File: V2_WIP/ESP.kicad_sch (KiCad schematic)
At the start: 41 parts, among them J202 USB4145-03-0230-C, J3 BATT, Q1 IRLML5203, Q2 S8050, Q3 S8050, SW3 FSM14JLH, SW4 FSM14JLH, U1 ESP32-WROOM-32E, U13 TP4057, U14 CH340K, U201 RT9080

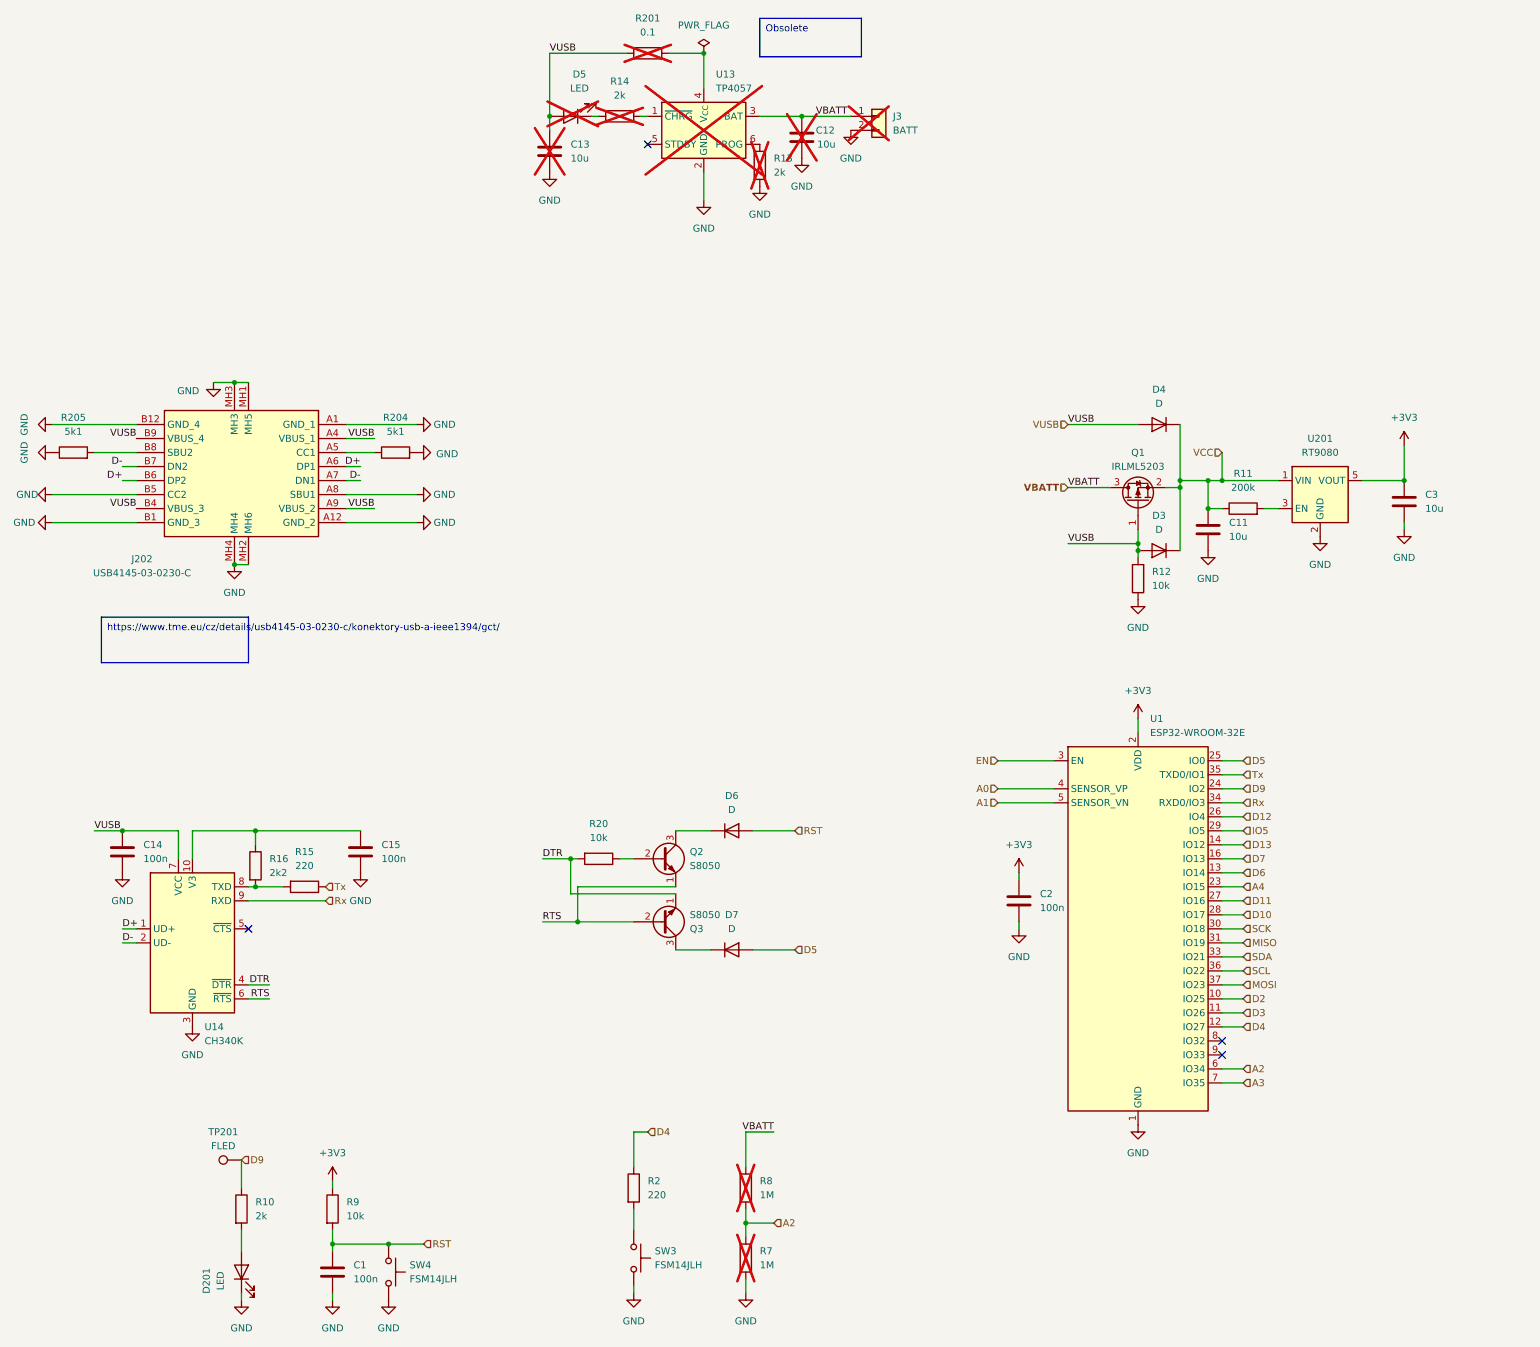
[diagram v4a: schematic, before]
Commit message: Removed EEPROM, Adjusted Flash connection, renamed ESP pins and several other signals
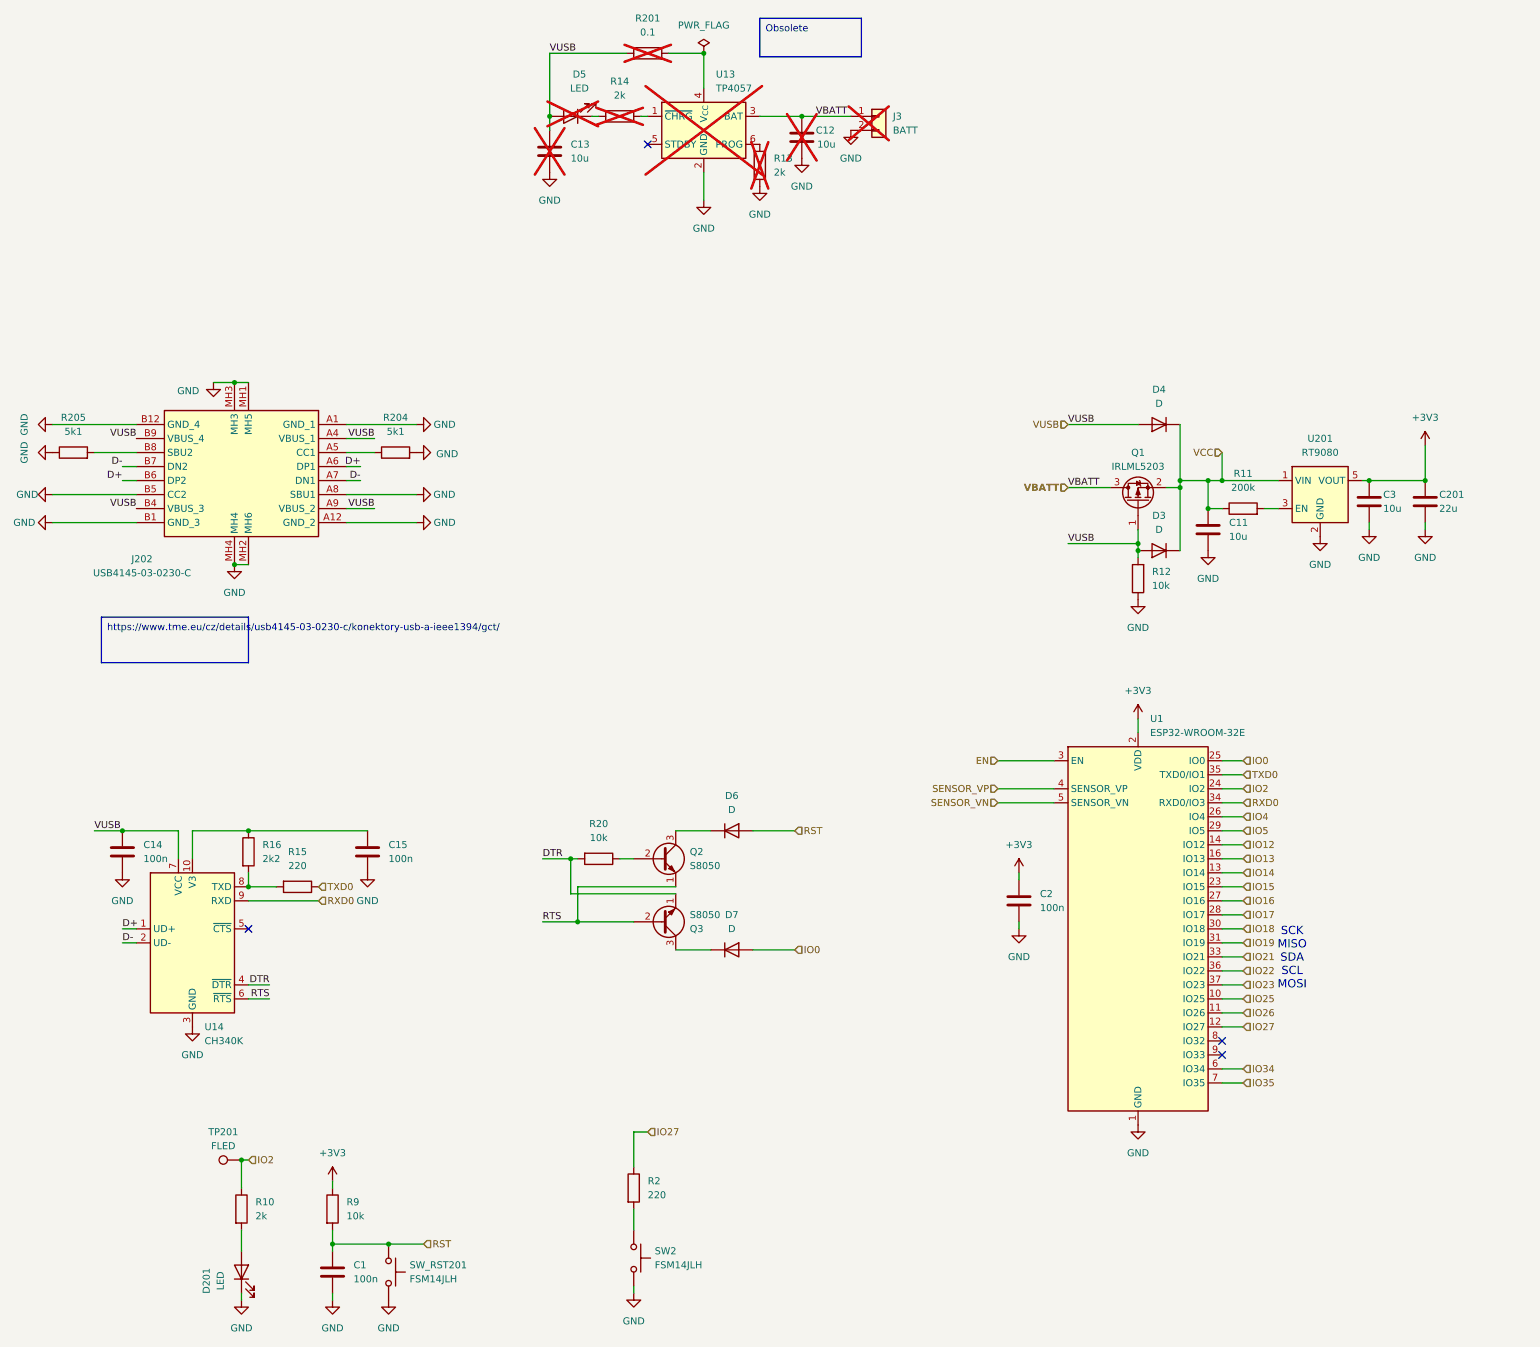
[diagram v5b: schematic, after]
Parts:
- removed R7, R8: 1M, Resistor_SMD:R_0603_1608Metric_Pad0.98x0.95mm_HandSolder, symbol Device:R
- added C201: 22u, Capacitor_SMD:C_0603_1608Metric_Pad1.08x0.95mm_HandSolder, symbol Device:C
- renumbered SW3 to SW2, SW4 to SW_RST201
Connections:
- net +3V3: now also C201.1
- net GND: now also C201.2
- net A0 renamed SENSOR_VP
- net A1 renamed SENSOR_VN
- net A2 renamed IO34
- net A3 renamed IO35
- net A4 renamed IO15
- net D10 renamed IO17
- net D11 renamed IO16
- net D12 renamed IO4
- net D13 renamed IO12
- net D2 renamed IO25
- net D3 renamed IO26
- net D4 renamed IO27
- net D5 renamed IO0
- net D6 renamed IO14
- net D7 renamed IO13
- net D9 renamed IO2
- net MISO renamed IO19
- net MOSI renamed IO23
- net Rx renamed RXD0
- net SCK renamed IO18
- net SCL renamed IO22
- net SDA renamed IO21
- net Tx renamed TXD0
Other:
- note added: "SCK MISO SDA SCL MOSI"
- moved on the sheet: C15, C3, R15, R16

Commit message: minor changes
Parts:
- removed SW_RST201: FSM14JLH, Button_Switch_THT:SW_PUSH_6mm, symbol Switch:SW_Push
- added R202: Manual rst, Resistor_SMD:R_0603_1608Metric_Pad0.98x0.95mm_HandSolder, symbol Device:R
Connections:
- net GND: now also R202.2
- net RST: now also R202.1
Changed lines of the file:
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@@
 	(wire
 		(pts
-			(xy 90.17 173.99) (xy 83.82 173.99)
-		)
-		(stroke
-			(width 0)
-			(type default)
-		)
-	)
-	(wire
-		(pts
 			(xy 234.95 129.54) (xy 238.76 129.54)
 		)
@@
 	(wire
 		(pts
+			(xy 83.82 175.26) (xy 83.82 173.99)
+		)
+		(stroke
+			(width 0)
+			(type default)
+		)
+	)
+	(wire
+		(pts
 			(xy 234.95 104.14) (xy 238.76 104.14)
 		)
@@
 	(wire
 		(pts
+			(xy 83.82 182.88) (xy 83.82 184.15)
+		)
+		(stroke
+			(width 0)
+			(type default)
+		)
+	)
+	(wire
+		(pts
 			(xy 45.72 99.06) (xy 45.72 104.14)
 		)
@@
 	(wire
 		(pts
+			(xy 83.82 173.99) (xy 90.17 173.99)
+		)
+		(stroke
+			(width 0)
+			(type default)
+		)
+	)
+	(wire
+		(pts
 			(xy 234.95 96.52) (xy 238.76 96.52)
 		)
@@
 		(exclude_from_sim no)
 		(at 31.75 60.325 0)
-		(size 26.67 8.255)
+		(size 89.154 8.255)
+		(stroke
+			(width 0)
+			(type default)
+		)
+		(fill
+			(type none)
+		)
+		(effects
+			(font
+				(size 1.27 1.27)
+			)
+			(justify left top)
+		)
+	)
+	(text_box "Manual rst possible by shorting R202"
+		(exclude_from_sim no)
+		(at 79.756 162.306 0)
+		(size 17.78 9.398)
 		(stroke
 			(width 0)
@@
 	)
 	(symbol
-		(lib_id "power:GND")
-		(at 151.13 -17.78 0)
+		(lib_id "Device:R")
+		(at 83.82 179.07 0)
 		(unit 1)
 		(exclude_from_sim no)
 		(in_bom yes)
 		(on_board yes)
-		(dnp no)
+		(dnp yes)
 		(fields_autoplaced yes)
-		(property "Reference" "#PWR0108"
-			(at 151.13 -11.43 0)
+		(property "Reference" "R202"
+			(at 86.36 177.7999 0)
 			(effects
 				(font
 					(size 1.27 1.27)
 				)
-				(hide yes)
+				(justify left)
 			)
 		)
-		(property "Value" "GND"
-			(at 151.13 -12.7 0)
+		(property "Value" "Manual rst"
+			(at 86.36 180.3399 0)
 			(effects
 				(font
 					(size 1.27 1.27)
 				)
+				(justify left)
 			)
 		)
-		(property "Footprint" ""
-			(at 151.13 -17.78 0)
+		(property "Footprint" "Resistor_SMD:R_0603_1608Metric_Pad0.98x0.95mm_HandSolder"
+			(at 82.042 179.07 90)
 			(effects
 				(font
@@
 			)
 		)
-		(property "Datasheet" ""
-			(at 151.13 -17.78 0)
+		(property "Datasheet" "~"
+			(at 83.82 179.07 0)
 			(effects
 				(font
@@
 			)
 		)
-		(property "Description" "Power symbol creates a global label with name \"GND\" , ground"
-			(at 151.13 -17.78 0)
+		(property "Description" "Resistor"
+			(at 83.82 179.07 0)
 			(effects
 				(font
@@
 		(pin "1"
 		)
+		(pin "2"
+		)
 		(instances
 			(project "gps"
 				(path "/00526ddc-5304-4072-af1e-192a9e7e83da/9ca8f2f0-17b3-4db3-a6cc-93c49e56ea8b"
-					(reference "#PWR0108")
+					(reference "R202")
 					(unit 1)
 				)
@@
 	(symbol
 		(lib_id "power:GND")
-		(at 232.41 48.26 0)
+		(at 151.13 -17.78 0)
 		(unit 1)
 		(exclude_from_sim no)
@@
 		(dnp no)
 		(fields_autoplaced yes)
-		(property "Reference" "#PWR0103"
-			(at 232.41 54.61 0)
+		(property "Reference" "#PWR0108"
+			(at 151.13 -11.43 0)
 			(effects
 				(font
@@
 		)
 		(property "Value" "GND"
-			(at 232.41 53.34 0)
+			(at 151.13 -12.7 0)
 			(effects
 				(font
@@
 		)
 		(property "Footprint" ""
-			(at 232.41 48.26 0)
+			(at 151.13 -17.78 0)
 			(effects
 				(font
@@
 		)
 		(property "Datasheet" ""
-			(at 232.41 48.26 0)
+			(at 151.13 -17.78 0)
 			(effects
 				(font
@@
 		)
 		(property "Description" "Power symbol creates a global label with name \"GND\" , ground"
-			(at 232.41 48.26 0)
+			(at 151.13 -17.78 0)
 			(effects
 				(font
@@
 			(project "gps"
 				(path "/00526ddc-5304-4072-af1e-192a9e7e83da/9ca8f2f0-17b3-4db3-a6cc-93c49e56ea8b"
-					(reference "#PWR0103")
+					(reference "#PWR0108")
 					(unit 1)
 				)
@@
 	)
 	(symbol
-		(lib_id "Switch:SW_Push")
-		(at 83.82 179.07 270)
+		(lib_id "power:GND")
+		(at 232.41 48.26 0)
 		(unit 1)
 		(exclude_from_sim no)
@@
 		(dnp no)
 		(fields_autoplaced yes)
-		(property "Reference" "SW_RST201"
-			(at 87.63 177.7999 90)
+		(property "Reference" "#PWR0103"
+			(at 232.41 54.61 0)
 			(effects
 				(font
 					(size 1.27 1.27)
 				)
-				(justify left)
+				(hide yes)
 			)
 		)
-		(property "Value" "FSM14JLH"
-			(at 87.63 180.3399 90)
+		(property "Value" "GND"
+			(at 232.41 53.34 0)
 			(effects
 				(font
 					(size 1.27 1.27)
 				)
-				(justify left)
 			)
 		)
-		(property "Footprint" "Button_Switch_THT:SW_PUSH_6mm"
-			(at 88.9 179.07 0)
+		(property "Footprint" ""
+			(at 232.41 48.26 0)
 			(effects
 				(font
@@
 			)
 		)
-		(property "Datasheet" "https://cz.mouser.com/ProductDetail/TE-Connectivity/FSM14JLH?qs=qzQkFgQjdxV0segVqkThUg%3D%3D"
-			(at 88.9 179.07 0)
+		(property "Datasheet" ""
+			(at 232.41 48.26 0)
 			(effects
 				(font
@@
 			)
 		)
-		(property "Description" "Push button switch, generic, two pins"
-			(at 83.82 179.07 0)
+		(property "Description" "Power symbol creates a global label with name \"GND\" , ground"
+			(at 232.41 48.26 0)
 			(effects
 				(font
@@
 			)
 		)
-		(pin "2"
-		)
 		(pin "1"
 		)
@@
 			(project "gps"
 				(path "/00526ddc-5304-4072-af1e-192a9e7e83da/9ca8f2f0-17b3-4db3-a6cc-93c49e56ea8b"
-					(reference "SW_RST201")
+					(reference "#PWR0103")
 					(unit 1)
 				)

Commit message: finallizes schematic; pcb progress
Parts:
- removed C1: 100n, Capacitor_SMD:C_0603_1608Metric_Pad1.08x0.95mm_HandSolder, symbol Device:C
- added C202: C_Polarized, Capacitor_SMD:C_Elec_6.3x7.7, symbol Device:C_Polarized
- added R203: 10k, Resistor_SMD:R_0603_1608Metric_Pad0.98x0.95mm_HandSolder, symbol Device:R
- added TP202: VCC, TestPoint:TestPoint_Pad_D1.5mm, symbol Connector:TestPoint
- D3, D4: value D -> M2; footprint Diode_SMD:D_0603_1608Metric_Pad1.05x0.95mm_HandSolder -> Diode_SMD:D_SMA
- D6, D7: value D -> 1N4148W-G3-08; footprint Diode_SMD:D_0603_1608Metric_Pad1.05x0.95mm_HandSolder -> Diode_SMD:D_SOD-123
- SW2: footprint Button_Switch_THT:SW_PUSH_6mm -> Button_Switch_SMD:SW_SPST_PTS647_Sx38
- U1: value ESP32-WROOM-32E -> ESP32-WROOM-32UE
- U201: value RT9080 -> RT9080-33GJ5
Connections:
- net EN is gone; now on net RST: U1.3 (EN)
- net +3V3: now also C202.1, R203.1
- net GND: now also C202.2
- net IO15: now also R2.1
- net IO27: no longer R2.1
- net VCC: now also TP202.1
- net at R2.2, SW2.1: now also R203.2
- net IO32: now reaches U1.8 (IO32)
- net IO34: no longer names the net of U1.6 (IO34)
- net IO5: no longer names the net of U1.29 (IO5)
- net SENSOR_VN: no longer names the net of U1.5 (SENSOR_VN)
- net SENSOR_VP: no longer names the net of U1.4 (SENSOR_VP)
- no-connect marks 4 -> 7
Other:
- moved on the sheet: C11, C201, C3, D3, D4, D6, D7, Q1, R11, R12, R202, U201

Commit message: updated most datashets
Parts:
- removed C12, C13: 10u, Capacitor_SMD:C_0603_1608Metric_Pad1.08x0.95mm_HandSolder, symbol Device:C
- removed D5: LED, Diode_SMD:D_0603_1608Metric_Pad1.05x0.95mm_HandSolder, symbol Device:LED
- removed J3: BATT, 1769:1769, symbol Connector_Generic:Conn_01x02
- removed R13, R14: 2k, Resistor_SMD:R_0603_1608Metric_Pad0.98x0.95mm_HandSolder, symbol Device:R
- removed R201: 0.1, Resistor_SMD:R_0603_1608Metric_Pad0.98x0.95mm_HandSolder, symbol Device:R
- removed U13: TP4057, Package_TO_SOT_SMD:SOT-23-6_Handsoldering, symbol Battery_Management:TP4057
- C11, C3: value 10u -> 10uF
- C14, C15, C2: value 100n -> 100nF
- C201: value 22u -> 22uF
- C202: value C_Polarized -> 470uF
- R16: value 2k2 -> 2k
- SW2: value FSM14JLH -> PTS647SN70SMTR2N LFS
- U14: value CH340K -> *CH340K
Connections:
- no-connect marks 7 -> 6
